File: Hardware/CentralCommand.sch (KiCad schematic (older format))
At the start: 1 part

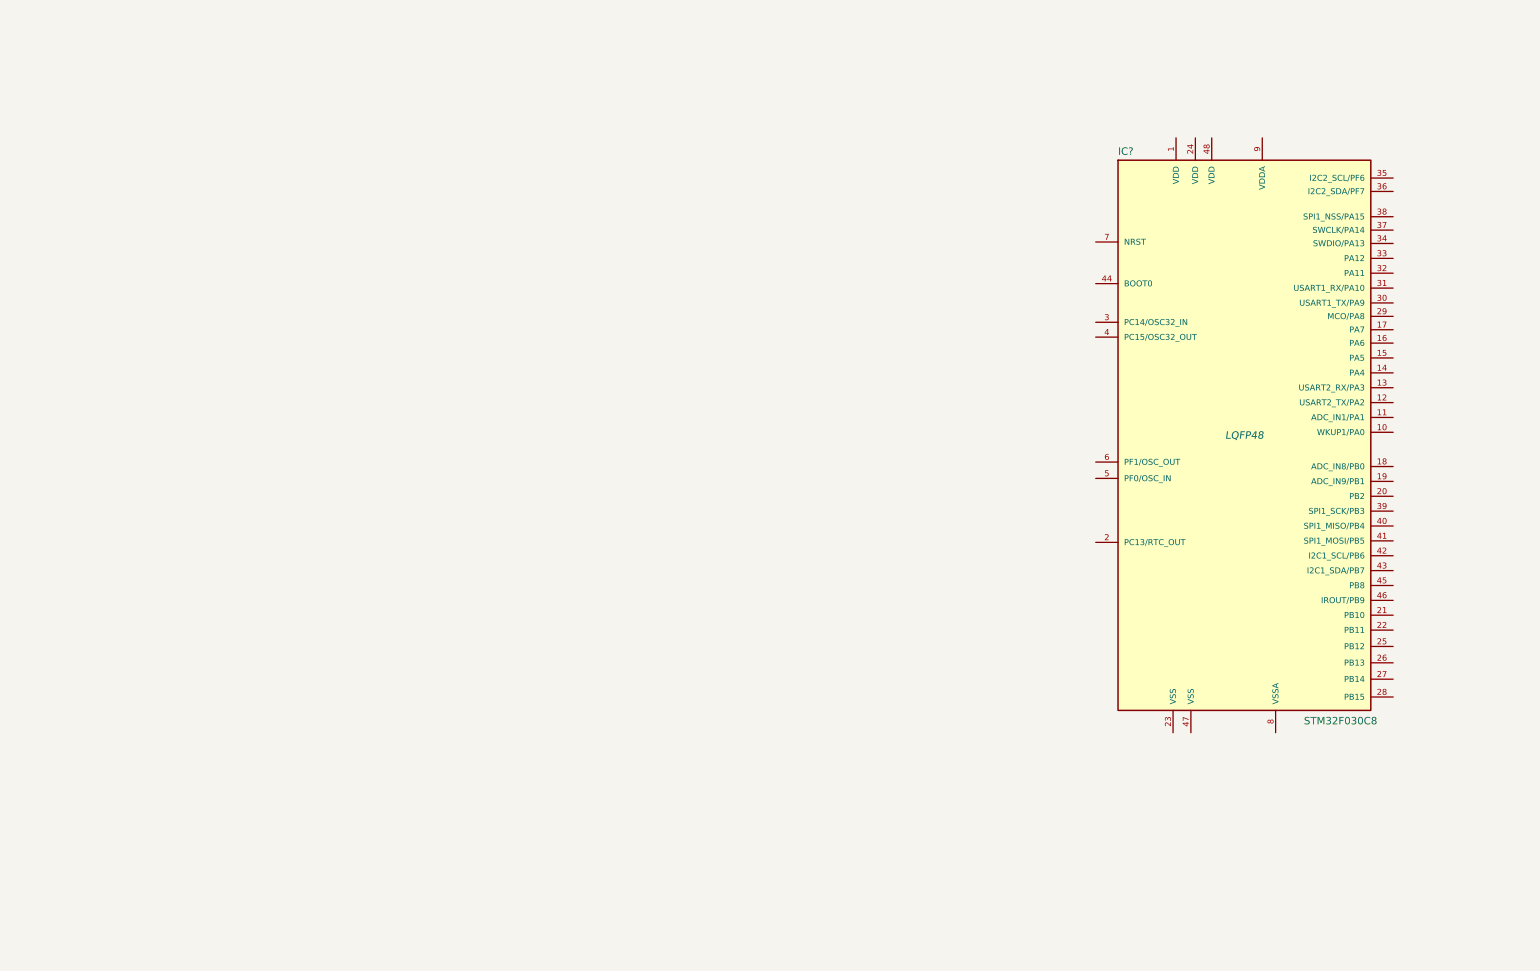
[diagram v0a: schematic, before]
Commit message: updated connectors and ftdi connections
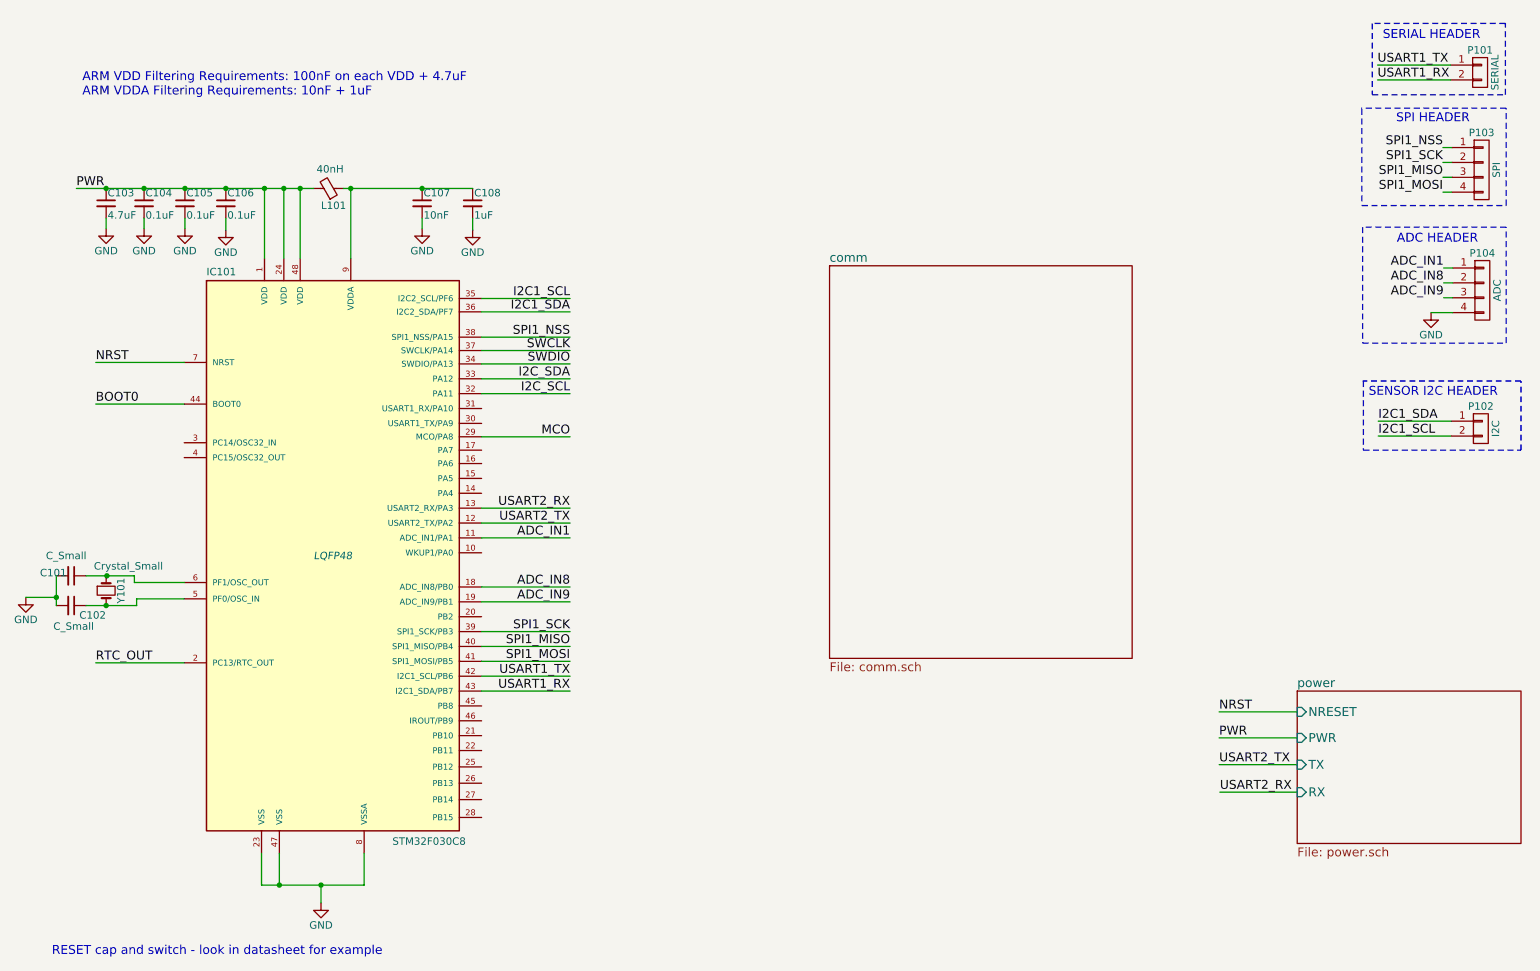
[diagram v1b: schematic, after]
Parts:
- removed IC?: STM32F030C8, LQFP48, symbol STM32F030C8
- added C101, C102: C_Small, symbol C_Small
- added C103: 4.7uF, symbol C_Small
- added C104, C105, C106: 0.1uF, symbol C_Small
- added C107: 10nF, symbol C_Small
- added C108: 1uF, symbol C_Small
- added IC101: STM32F030C8, LQFP48, symbol STM32F030C8
- added L101: 40nH, symbol Ferrite_Bead_Small
- added P101: SERIAL, symbol CONN_01X02
- added P102: I2C, symbol CONN_01X02
- added P103: SPI, symbol CONN_01X04
- added P104: ADC, symbol CONN_01X04
- added Y101: Crystal_Small, symbol Crystal_Small
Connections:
- new net: C107.1, C108.1, IC101.9 (VDDA), L101.1
- new net: C101.1, IC101.6 (PF1/OSC_OUT), Y101.1
- new net: C102.1, IC101.5 (PF0/OSC_IN), Y101.2
- new net ADC_IN1: IC101.11 (ADC_IN1/PA1), P104.1 (P1)
- new net ADC_IN8: IC101.18 (ADC_IN8/PB0), P104.2 (P2)
- new net ADC_IN9: IC101.19 (ADC_IN9/PB1), P104.3 (P3)
- new net BOOT0: IC101.44 (BOOT0)
- new net GND: C101.2, C102.2, C103.2, C104.2, C105.2, C106.2, C107.2, C108.2, IC101.23 (VSS), IC101.47 (VSS), IC101.8 (VSSA), P104.4 (P4)
- new net I2C1_SCL: IC101.35 (I2C2_SCL/PF6), P102.2 (P2)
- new net I2C1_SDA: IC101.36 (I2C2_SDA/PF7), P102.1 (P1)
- new net I2C_SCL: IC101.32 (PA11)
- new net I2C_SDA: IC101.33 (PA12)
- new net MCO: IC101.29 (MCO/PA8)
- new net NRST: IC101.7 (NRST)
- new net PWR: C103.1, C104.1, C105.1, C106.1, IC101.1 (VDD), IC101.24 (VDD), IC101.48 (VDD), L101.2
- new net RTC_OUT: IC101.2 (PC13/RTC_OUT)
- new net SPI1_MISO: IC101.40 (SPI1_MISO/PB4), P103.3 (P3)
- new net SPI1_MOSI: IC101.41 (SPI1_MOSI/PB5), P103.4 (P4)
- new net SPI1_NSS: IC101.38 (SPI1_NSS/PA15), P103.1 (P1)
- new net SPI1_SCK: IC101.39 (SPI1_SCK/PB3), P103.2 (P2)
- new net SWCLK: IC101.37 (SWCLK/PA14)
- new net SWDIO: IC101.34 (SWDIO/PA13)
- new net USART1_RX: IC101.43 (I2C1_SDA/PB7), P101.2 (P2)
- new net USART1_TX: IC101.42 (I2C1_SCL/PB6), P101.1 (P1)
- new net USART2_RX: IC101.13 (USART2_RX/PA3)
- new net USART2_TX: IC101.12 (USART2_TX/PA2)
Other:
- note added: "ADC HEADER"
- note added: "ARM VDD Filtering Requirements: 100nF on each VDD + 4.7uF\nARM VDDA Filtering Requirements: 10nF + 1uF"
- note added: "RESET cap and switch - look in datasheet for example"
- note added: "SENSOR I2C HEADER"
- note added: "SERIAL HEADER"
- note added: "SPI HEADER"

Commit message: reassigned pin to correct I2C1, I2C2, and USART1 connections
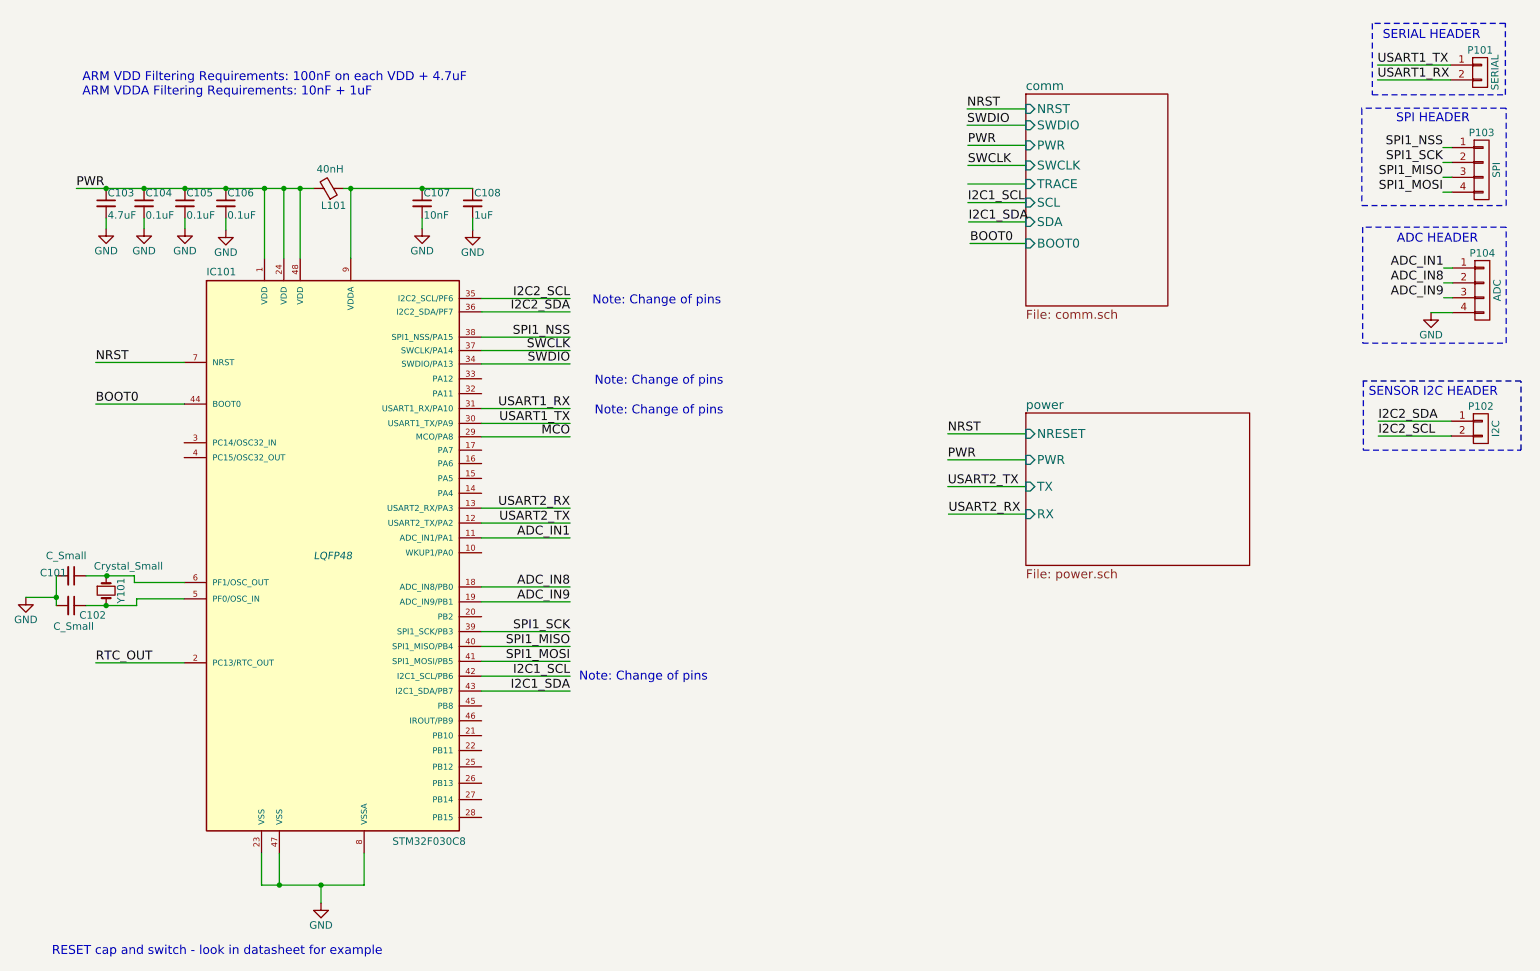
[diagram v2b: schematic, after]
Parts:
- IC101: Fieldname (none) -> Value
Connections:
- net I2C1_SCL: now also IC101.42 (I2C1_SCL/PB6); no longer IC101.35 (I2C2_SCL/PF6), P102.2 (P2)
- net I2C1_SDA: now also IC101.43 (I2C1_SDA/PB7); no longer IC101.36 (I2C2_SDA/PF7), P102.1 (P1)
- net USART1_RX: now also IC101.31 (USART1_RX/PA10); no longer IC101.43 (I2C1_SDA/PB7)
- net USART1_TX: now also IC101.30 (USART1_TX/PA9); no longer IC101.42 (I2C1_SCL/PB6)
- net I2C_SCL: no longer names the net of IC101.32 (PA11)
- net I2C_SDA: no longer names the net of IC101.33 (PA12)
- new net I2C2_SCL: IC101.35 (I2C2_SCL/PF6), P102.2 (P2)
- new net I2C2_SDA: IC101.36 (I2C2_SDA/PF7), P102.1 (P1)
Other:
- note added: "Note: Change of pins"
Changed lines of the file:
@@
 LIBS:contrib
 LIBS:valves
+LIBS:switches
+LIBS:stm32
 LIBS:CentralCommand-cache
 EELAYER 25 0
@@
 $EndDescr
 $Sheet
-S 9455 5180 1505 1025
+S 7630 3310 1505 1025
 U 58D7AFB1
 F0 "power" 60
 F1 "power.sch" 60
-F2 "PWR" I L 9455 5495 60
-F3 "NRESET" I L 9455 5320 60
-F4 "TX" I L 9455 5675 60
-F5 "RX" I L 9455 5860 60
+F2 "PWR" I L 7630 3625 60
+F3 "NRESET" I L 7630 3450 60
+F4 "TX" I L 7630 3805 60
+F5 "RX" I L 7630 3990 60
 $EndSheet
 $Comp
@@
 PWR
 Wire Wire Line
-	9455 5495 8930 5495
-Text Label 8930 5495 0    60   ~ 0
+	7630 3625 7105 3625
+Text Label 7105 3625 0    60   ~ 0
 PWR
 Wire Wire Line
@@
 Wire Wire Line
 	3970 2540 4565 2540
-Text Label 4565 2540 2    60   ~ 0
+Text Label 4565 5080 2    60   ~ 0
 I2C1_SCL
 Wire Wire Line
 	3970 2630 4565 2630
-Text Label 4565 2630 2    60   ~ 0
+Text Label 4565 5180 2    60   ~ 0
 I2C1_SDA
 Wire Wire Line
@@
 Text Label 4565 4150 2    60   ~ 0
 ADC_IN1
-Wire Wire Line
-	3970 3180 4565 3180
-Text Label 4565 3180 2    60   ~ 0
-I2C_SCL
-Wire Wire Line
-	3970 3080 4565 3080
-Text Label 4565 3080 2    60   ~ 0
-I2C_SDA
+Text Label 4565 2540 2    60   ~ 0
+I2C2_SCL
+Text Label 4565 2630 2    60   ~ 0
+I2C2_SDA
 Wire Wire Line
 	3970 2980 4565 2980
@@
 Wire Wire Line
 	3970 5080 4565 5080
-Text Label 4565 5080 2    60   ~ 0
+Text Label 4565 3380 2    60   ~ 0
 USART1_TX
 Wire Wire Line
 	3970 5180 4565 5180
-Text Label 4565 5180 2    60   ~ 0
+Text Label 4565 3280 2    60   ~ 0
 USART1_RX
 Text Notes 1285 1185 0    60   ~ 0
@@
 	10000 3465 10490 3465
 Text Label 10000 3365 0    60   ~ 0
-I2C1_SDA
+I2C2_SDA
 Text Label 10000 3465 0    60   ~ 0
-I2C1_SCL
+I2C2_SCL
 Text Notes 9935 3205 0    60   ~ 0
 SENSOR I2C HEADER
@@
 	10960 3095 9895 3095
 $Sheet
-S 6310 2320 2035 2640
+S 7630 1165 955  1425
 U 58DEA2CA
 F0 "comm" 60
 F1 "comm.sch" 60
+F2 "PWR" I L 7630 1510 60
+F3 "SWCLK" I L 7630 1645 60
+F4 "SWDIO" I L 7630 1375 60
+F5 "NRST" I L 7630 1265 60
+F6 "TRACE" I L 7630 1770 60
+F7 "SCL" I L 7630 1895 60
+F8 "SDA" I L 7630 2025 60
+F9 "BOOT0" I L 7630 2170 60
 $EndSheet
 Wire Wire Line
-	8930 5675 9455 5675
-Wire Wire Line
-	9455 5860 8935 5860
-Text Label 8930 5675 0    60   ~ 0
+	7105 3805 7630 3805
+Wire Wire Line
+	7630 3990 7110 3990
+Text Label 7105 3805 0    60   ~ 0
 USART2_TX
-Text Label 8935 5860 0    60   ~ 0
+Text Label 7110 3990 0    60   ~ 0
 USART2_RX
-Text Label 8930 5320 0    60   ~ 0
+Text Label 7105 3450 0    60   ~ 0
 NRST
 Wire Wire Line
-	9455 5320 8930 5320
+	7630 3450 7105 3450
 $Comp
 L STM32F030C8 IC101
@@
 F 1 "STM32F030C8" H 3370 2320 50  0000 L BNN
 F 2 "LQFP48" H 2970 4270 50  0000 C CIN
-F 3 "" H 2970 4270 50  0000 C CNN
+F 3 "http://www.st.com/content/ccc/resource/technical/document/datasheet/a4/5d/0b/0e/87/c4/4d/71/DM00088500.pdf/files/DM00088500.pdf/jcr:content/translations/en.DM00088500.pdf" H 2970 4270 50  0001 C CNN
+F 4 "Value" H 2970 4270 60  0001 C CNN "Fieldname"
 	1    2970 4270
 	1    0    0    -1
 $EndComp
+Wire Wire Line
+	7630 1265 7235 1265
+Wire Wire Line
+	7630 1375 7235 1375
+Wire Wire Line
+	7630 1510 7240 1510
+Wire Wire Line
+	7630 1645 7240 1645
+Wire Wire Line
+	7630 1770 7240 1770
+Wire Wire Line
+	7240 1895 7630 1895
+Wire Wire Line
+	7630 2025 7245 2025
+Text Label 7240 1510 0    60   ~ 0
+PWR
+Text Label 7235 1375 0    60   ~ 0
+SWDIO
+Text Label 7240 1645 0    60   ~ 0
+SWCLK
+Text Label 7245 2025 0    60   ~ 0
+I2C1_SDA
+Text Label 7240 1895 0    60   ~ 0
+I2C1_SCL
+Text Label 7235 1265 0    60   ~ 0
+NRST
+Wire Wire Line
+	7630 2170 7255 2170
+Text Label 7255 2170 0    60   ~ 0
+BOOT0
+Text Notes 4625 5120 0    60   ~ 0
+Note: Change of pins
+Text Notes 4715 2590 0    60   ~ 0
+Note: Change of pins
+Wire Wire Line
+	3970 3280 4565 3280
+Wire Wire Line
+	3970 3380 4565 3380
+Text Notes 4730 3330 0    60   ~ 0
+Note: Change of pins
+Text Notes 4730 3130 0    60   ~ 0
+Note: Change of pins
 $EndSCHEMATC
